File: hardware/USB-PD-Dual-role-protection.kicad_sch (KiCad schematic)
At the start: 12 parts, among them J2 USB_C_Receptacle_USB2.0, Q1 STL40DN3LLH, Q2 DMT3020LDV, U3 TCPP03-M20

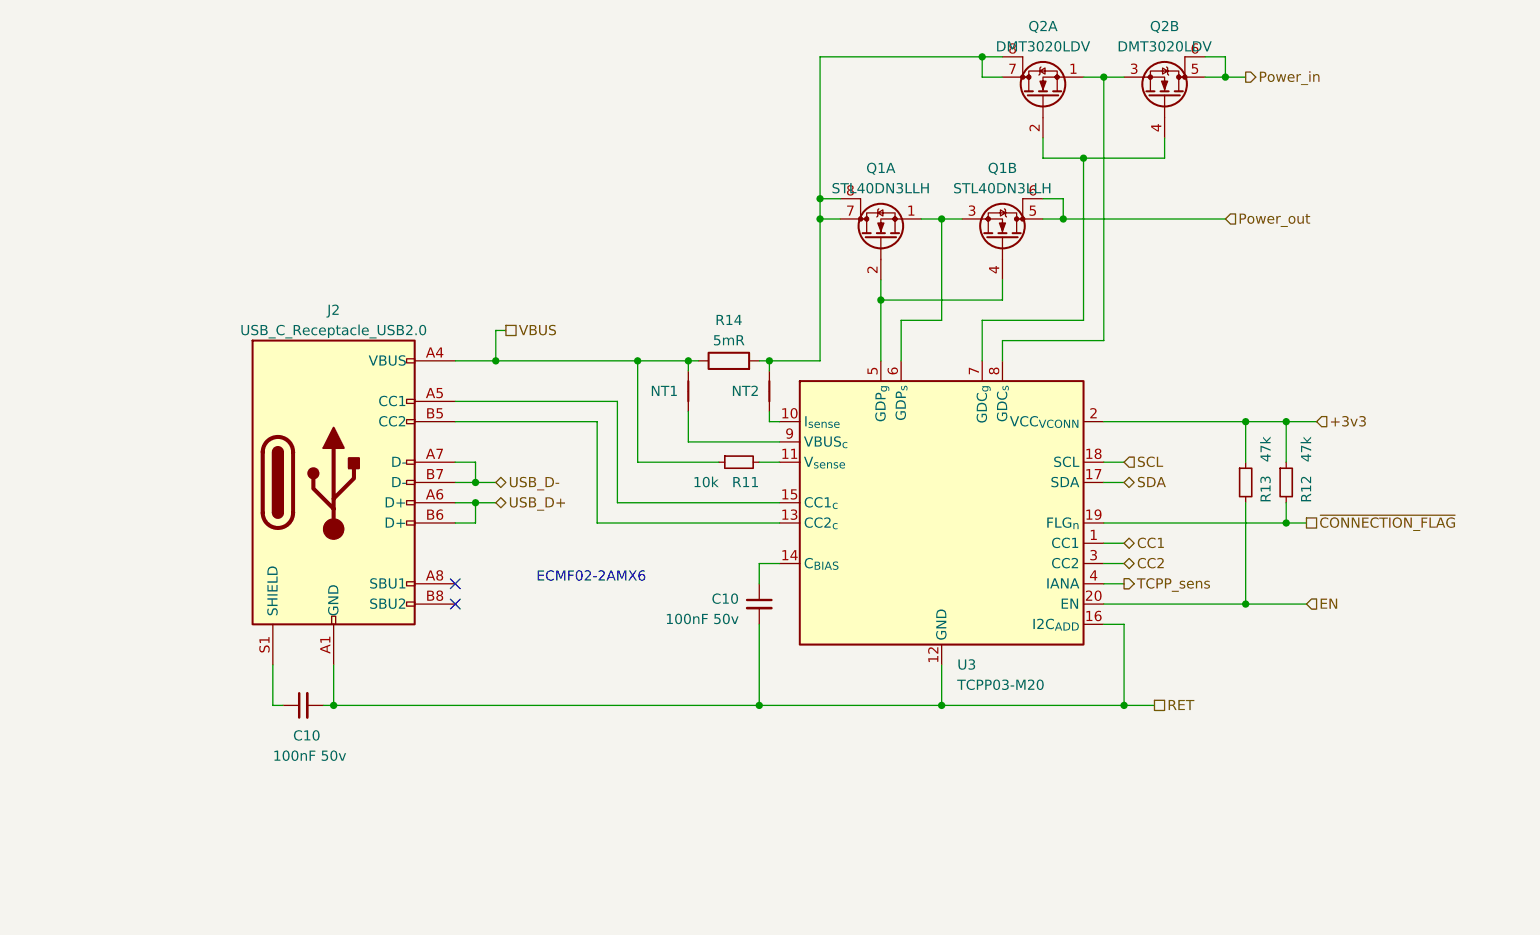
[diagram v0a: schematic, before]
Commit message: Added BMS and DC/DC
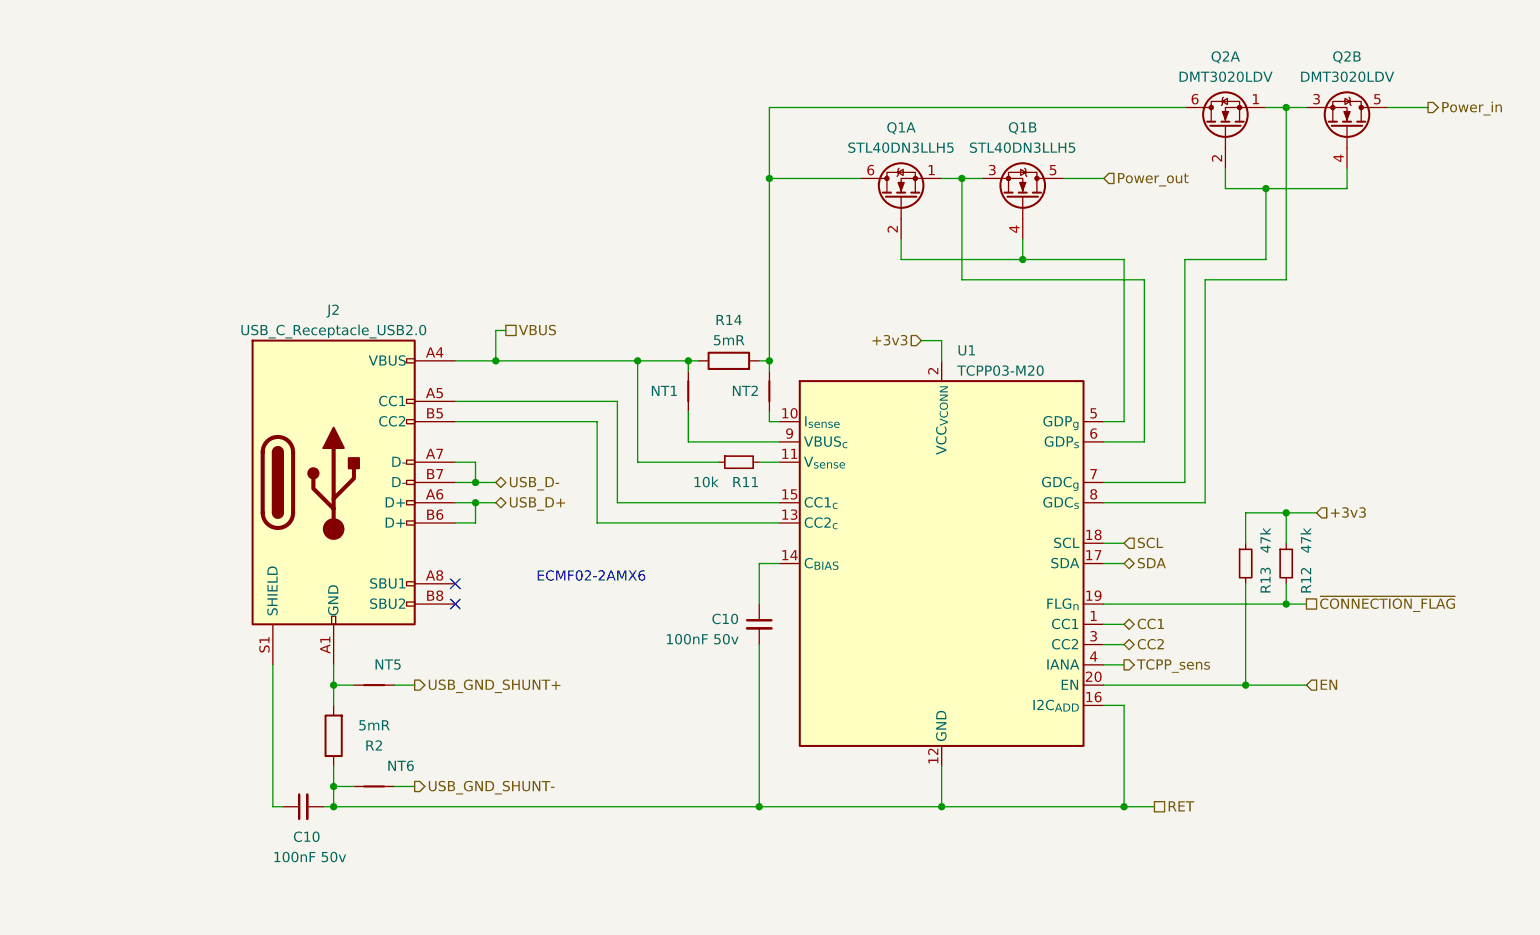
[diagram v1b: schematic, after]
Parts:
- removed Q1: STL40DN3LLH, Package_DFN_QFN:PQFN-8-EP_6x5mm_P1.27mm_Generic, symbol Device:Q_Dual_NMOS_S1G1S2G2D2D2D1D1
- removed Q2: DMT3020LDV, Package_SON:VSON-8_3.3x3.3mm_P0.65mm_NexFET, symbol Device:Q_Dual_NMOS_S1G1S2G2D2D2D1D1
- removed U3: TCPP03-M20, Package_DFN_QFN:QFN-20-1EP_4x4mm_P0.5mm_EP2.1x2.1mm, symbol Power_Management:TCPP03-M20
- added NT5, NT6: NetTie_2, NetTie:NetTie-2_SMD_Pad0.5mm, symbol Device:NetTie_2
- added Q1: STL40DN3LLH5, symbol Device:Q_Dual_NMOS_S1G1S2G2D2D1
- added Q2: DMT3020LDV, Package_DFN_QFN:Diodes_PowerDI3333-8_UXC_DFN-8_3.3x3.3mm_P0.65mm, symbol Device:Q_Dual_NMOS_S1G1S2G2D2D1
- added R2: 5mR, Resistor_SMD:R_1206_3216Metric, symbol Device:R
- added U1: TCPP03-M20, Package_DFN_QFN:TQFN-20-1EP_4x4mm_P0.5mm_EP2.1x2.1mm, symbol Power_Protection:TCPP03-M20
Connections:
- net +3v3: now also U1.2 (VCC_{VCONN})
- net CC1: now also U1.1 (CC1)
- net CC2: now also U1.3 (CC2)
- net EN: now also U1.20 (EN)
- net Power_in: now also Q2.5 (D)
- net Power_out: now also Q1.5 (D)
- net RET: now also NT6.1, R2.1, U1.12 (GND), U1.16 (I2C_{ADD}), U1.21 (GND); no longer J2.A1 (GND), J2.A12 (GND), J2.B1 (GND), J2.B12 (GND)
- net SCL: now also U1.18 (SCL)
- net SDA: now also U1.17 (SDA)
- net TCPP_sens: now also U1.4 (IANA)
- net ~{CONNECTION_FLAG}: now also U1.19 (FLG_{n})
- net at R11.2: now also U1.11 (V_{sense})
- net at NT1.1: now also U1.9 (VBUS_{c})
- net at NT2.2, R14.2: now also Q1.6 (D), Q2.6 (D)
- net at NT2.1: now also U1.10 (I_{sense})
- net at J2.B5 (CC2): now also U1.13 (CC2_{c})
- net at C10.1: now also U1.14 (C_{BIAS})
- net at J2.A5 (CC1): now also U1.15 (CC1_{c})
- new net: J2.A1 (GND), J2.A12 (GND), J2.B1 (GND), J2.B12 (GND), NT5.2, R2.2
- new net: Q1.2 (G), Q1.4 (G), U1.5 (GDP_{g})
- new net: Q1.1 (S), Q1.3 (S), U1.6 (GDP_{s})
- new net: Q2.2 (G), Q2.4 (G), U1.7 (GDC_{g})
- new net: Q2.1 (S), Q2.3 (S), U1.8 (GDC_{s})
- new net USB_GND_SHUNT+: NT5.1
- new net USB_GND_SHUNT-: NT6.2
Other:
- moved on the sheet: C10, R12, R13

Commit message: Some routing and pinout changes
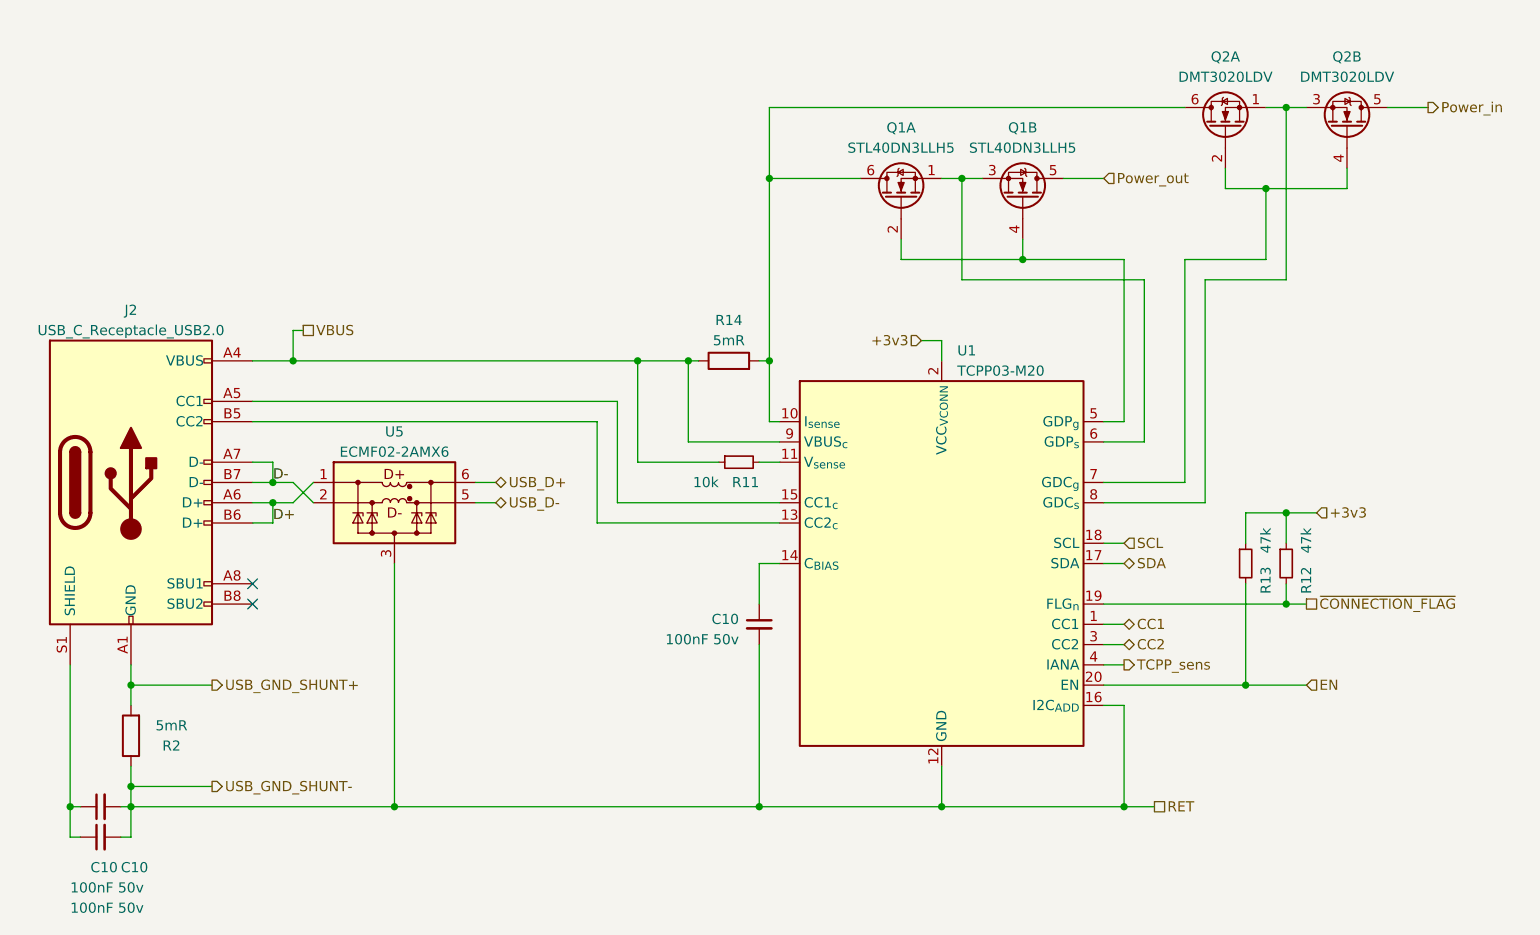
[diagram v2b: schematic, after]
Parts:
- removed NT1, NT2, NT5, NT6: NetTie_2, NetTie:NetTie-2_SMD_Pad0.5mm, symbol Device:NetTie_2
- added C10: 100nF 50v, Capacitor_SMD:C_0402_1005Metric, symbol Device:C_Small
- added U5: ECMF02-2AMX6, Package_DFN_QFN:ST_UQFN-6L_1.5x1.7mm_Pitch0.5mm, symbol Power_Protection:ECMF02-2AMX6
- C10: footprint (none) -> Capacitor_SMD:C_0402_1005Metric
- Q1: footprint (none) -> Package_SON:ST_PowerFLAT-6L_5x6mm_P1.27mm
- Q2: footprint Package_DFN_QFN:Diodes_PowerDI3333-8_UXC_DFN-8_3.3x3.3mm_P0.65mm -> Package_SON:Diodes_PowerDI3333-8_UXC_3.3x3.3mm_P0.65mm
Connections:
- net RET: now also C10.2, U5.3 (GND)
- net USB_D+: now also U5.6 (D+_out); no longer J2.A6 (D+), J2.B6 (D+)
- net USB_D-: now also U5.5 (D-_out); no longer J2.A7 (D-), J2.B7 (D-)
- net USB_GND_SHUNT+: now also J2.A1 (GND), J2.A12 (GND), J2.B1 (GND), J2.B12 (GND), R2.2
- net VBUS: now also U1.9 (VBUS_{c})
- net at U1.10 (I_{sense}): now also Q1.6 (D), Q2.6 (D), R14.2
- net at C10.1, J2.S1 (SHIELD): now also C10.1
- new net D+: J2.A6 (D+), J2.B6 (D+), U5.1 (D+_in)
- new net D-: J2.A7 (D-), J2.B7 (D-), U5.2 (D-_in)
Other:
- note removed: "ECMF02-2AMX6"
- moved on the sheet: C10, J2, R2
